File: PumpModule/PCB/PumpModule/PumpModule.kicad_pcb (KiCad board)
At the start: 2 copper layers, 55 x 105 mm, 12 parts, among them J5 Bus, J6 Motor, J7 Switch

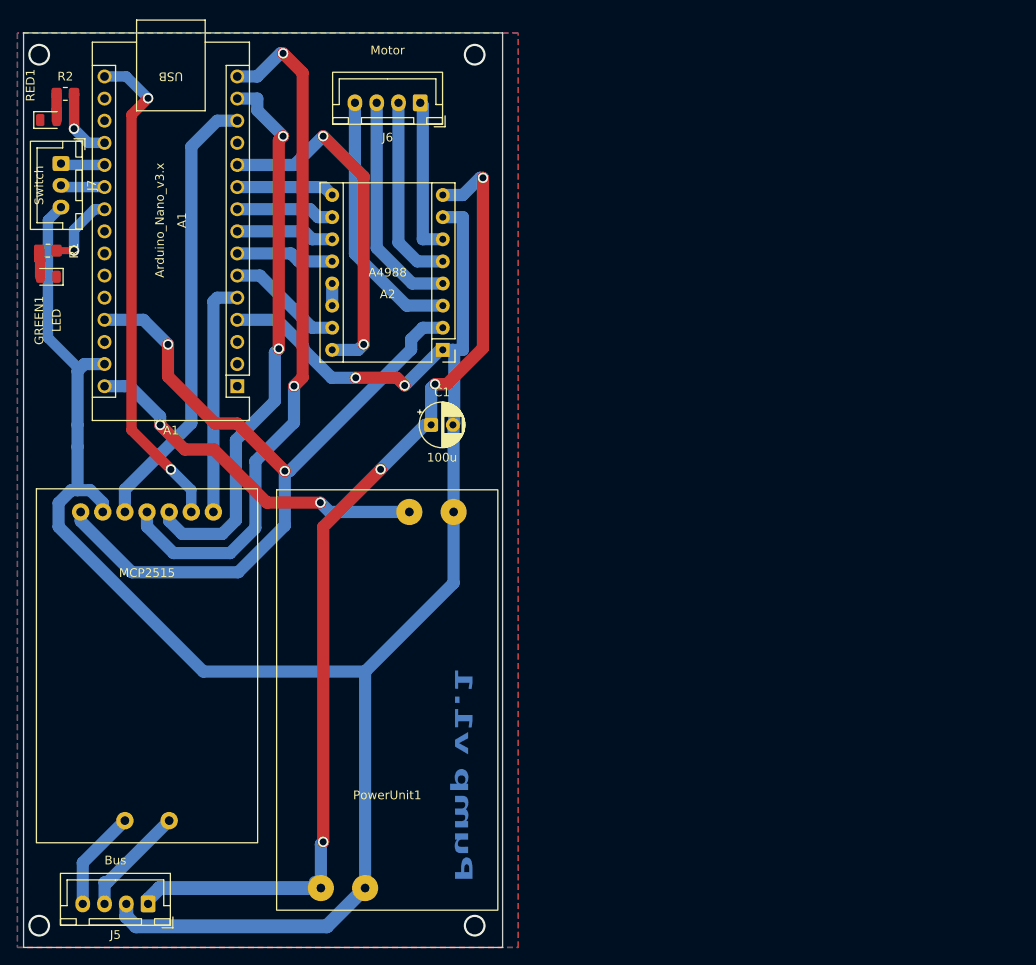
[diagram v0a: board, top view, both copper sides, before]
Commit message: [PumpModule][PCB] Add Manufacturing files for 2 PumpModule v1.1 on board
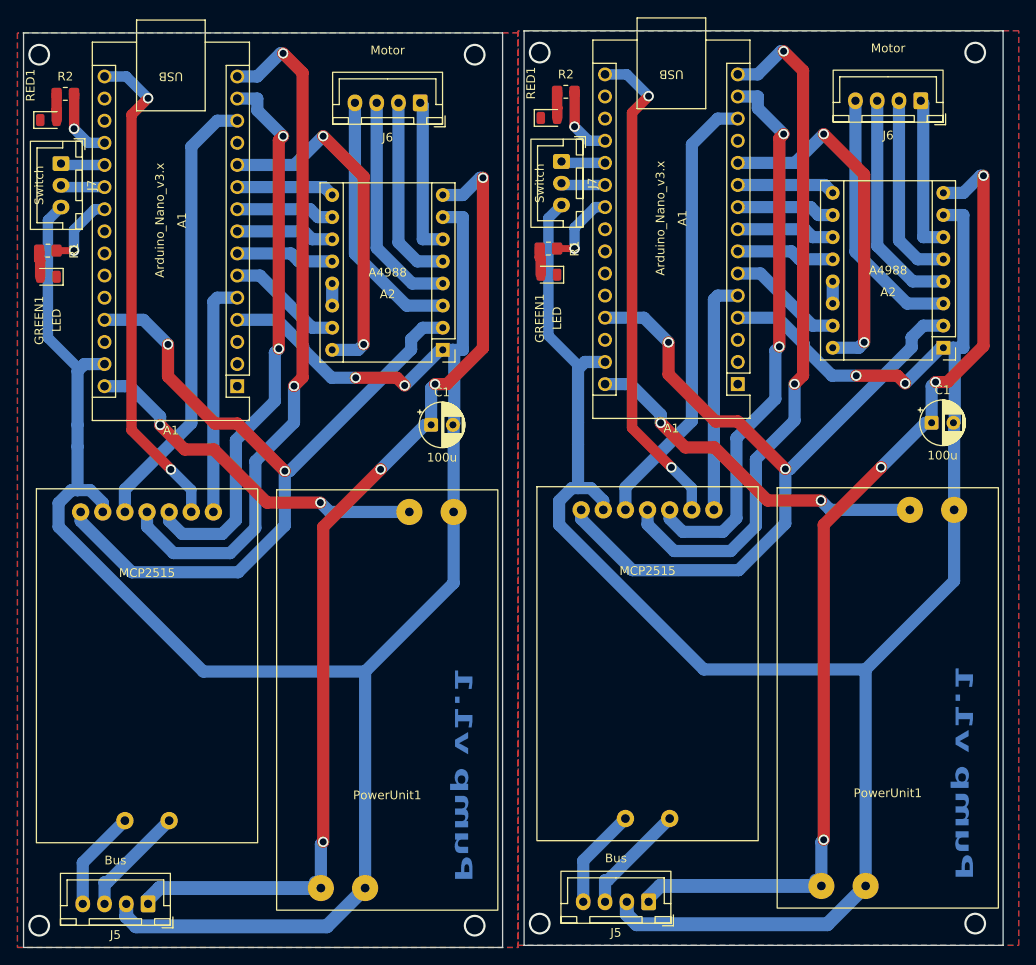
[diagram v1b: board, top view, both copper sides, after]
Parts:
- added A1: Arduino_Nano_v3.x, Module:Arduino_Nano, F.Cu at (120.2, 70.3)
- added A2: A4988, Module:Pololu_Breakout-16_15.2x20.3mm, F.Cu at (143.8, 66.2)
- added C1: 100u, Capacitor_THT:CP_Radial_D5.0mm_P2.50mm, F.Cu at (142.5, 74.8)
- added GREEN1: LED, LED_SMD:LED_0805_2012Metric, F.Cu at (98.5, 57.8)
- added J5: Bus, Connector_JST:JST_XH_B4B-XH-A_1x04_P2.50mm_Vertical, F.Cu at (110.0, 129.8)
- added J6: Motor, Connector_JST:JST_XH_B4B-XH-A_1x04_P2.50mm_Vertical, F.Cu at (141.2, 37.8)
- added J7: Switch, Connector_JST:JST_XH_B3B-XH-A_1x03_P2.50mm_Vertical, F.Cu at (100.0, 44.8)
- added MCP2515: ~, PumpModule:MCP2515Mudule, F.Cu at (109.8, 92.3)
- added PowerUnit1: ~, PumpModule:DC-DC_Low, F.Cu at (137.4, 117.8)
- added R1: R, Resistor_SMD:R_0805_2012Metric_Pad1.20x1.40mm_HandSolder, F.Cu at (98.5, 54.8)
- added R2: R, Resistor_SMD:R_0805_2012Metric_Pad1.20x1.40mm_HandSolder, F.Cu at (100.5, 36.8)
- added RED1: LED, LED_SMD:LED_0805_2012Metric, F.Cu at (98.5, 39.8)
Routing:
- net GND: track 235.9 -> 471.8 mm, vias 2 -> 4
- net +12V: track 117.7 -> 235.5 mm, vias 4 -> 8
- net +5V: track 91.1 -> 182.2 mm, vias 2 -> 4
- net Net-(A1-D12): track 80.6 -> 161.2 mm, vias 2 -> 4
- net Net-(A1-D11): track 64.1 -> 128.3 mm, vias 2 -> 4
- net Net-(A1-D13): track 57.2 -> 114.3 mm, vias 2 -> 4
- net Net-(A1-D10): track 51.6 -> 103.2 mm
- net Net-(A1-VIN): track 41.5 -> 83.1 mm, vias 2 -> 4
- net Net-(A1-D8): track 40.9 -> 81.9 mm, vias 2 -> 4
- net Net-(A2-1B): track 29.9 -> 59.8 mm
- net Net-(A1-D2): track 27.1 -> 54.2 mm
- net Net-(A2-1A): track 25.9 -> 51.9 mm
- net Net-(A2-2A): track 22.0 -> 44.1 mm
- net Net-(A2-2B): track 18.1 -> 36.2 mm
- net Net-(A1-D3): track 13.4 -> 26.8 mm
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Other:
- board size 55 x 105 mm -> 112.5 x 105.2 mm
